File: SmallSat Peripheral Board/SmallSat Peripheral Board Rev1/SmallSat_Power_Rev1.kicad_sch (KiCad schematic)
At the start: 17 parts

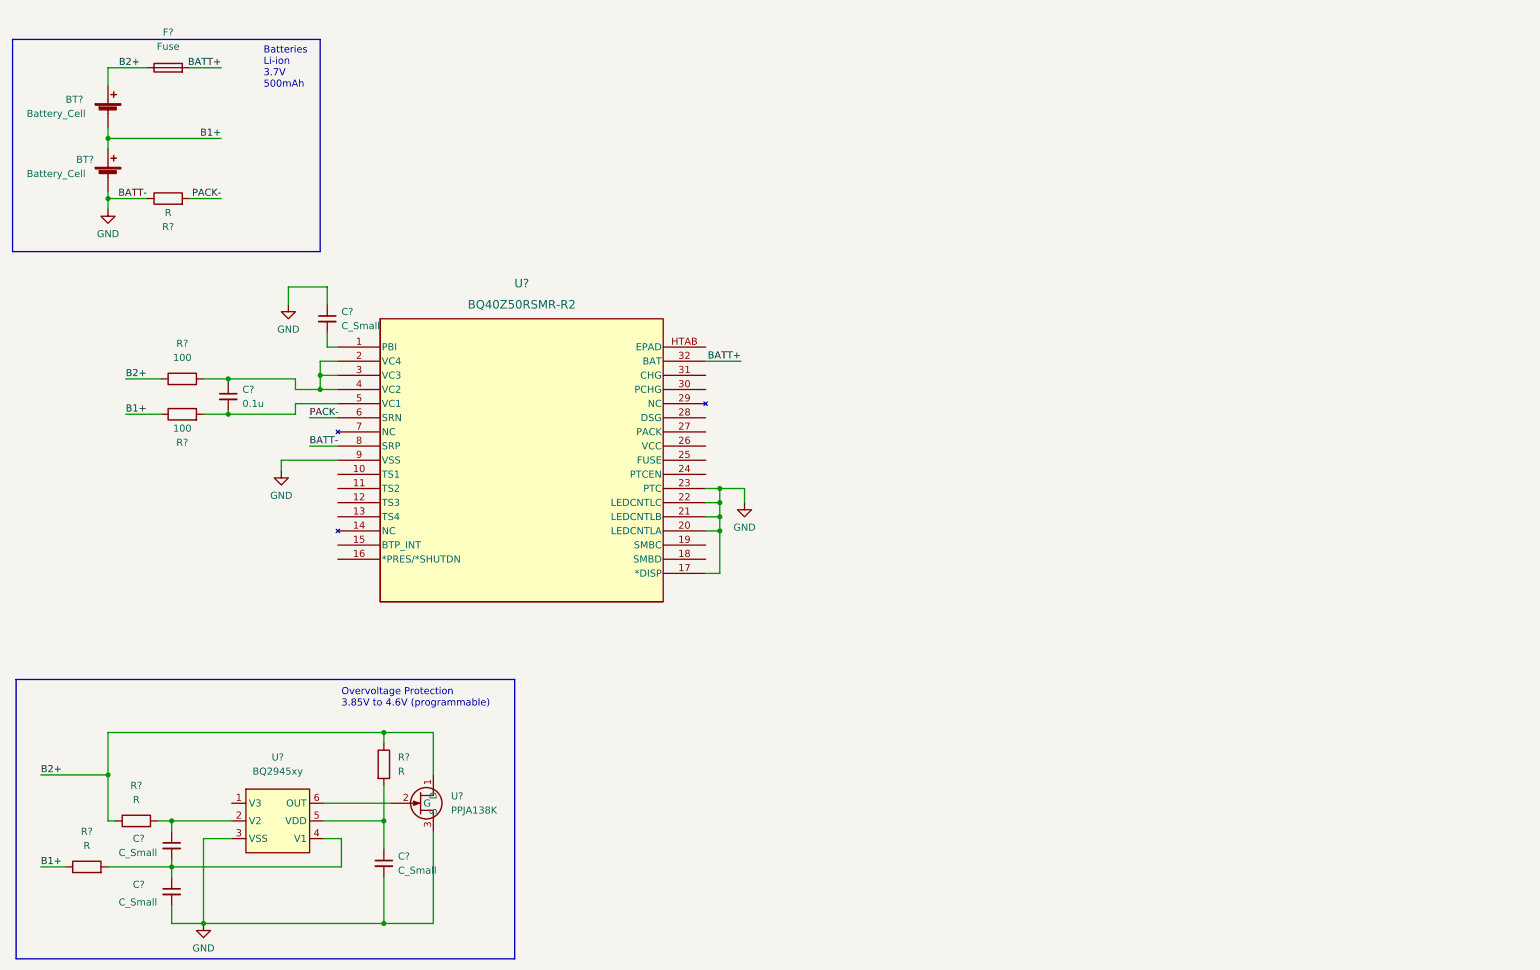
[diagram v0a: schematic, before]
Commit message: Updated Power Section
Now using BQ28Z620DRZR fuel gauge
Now using BQ296202DSGR protection
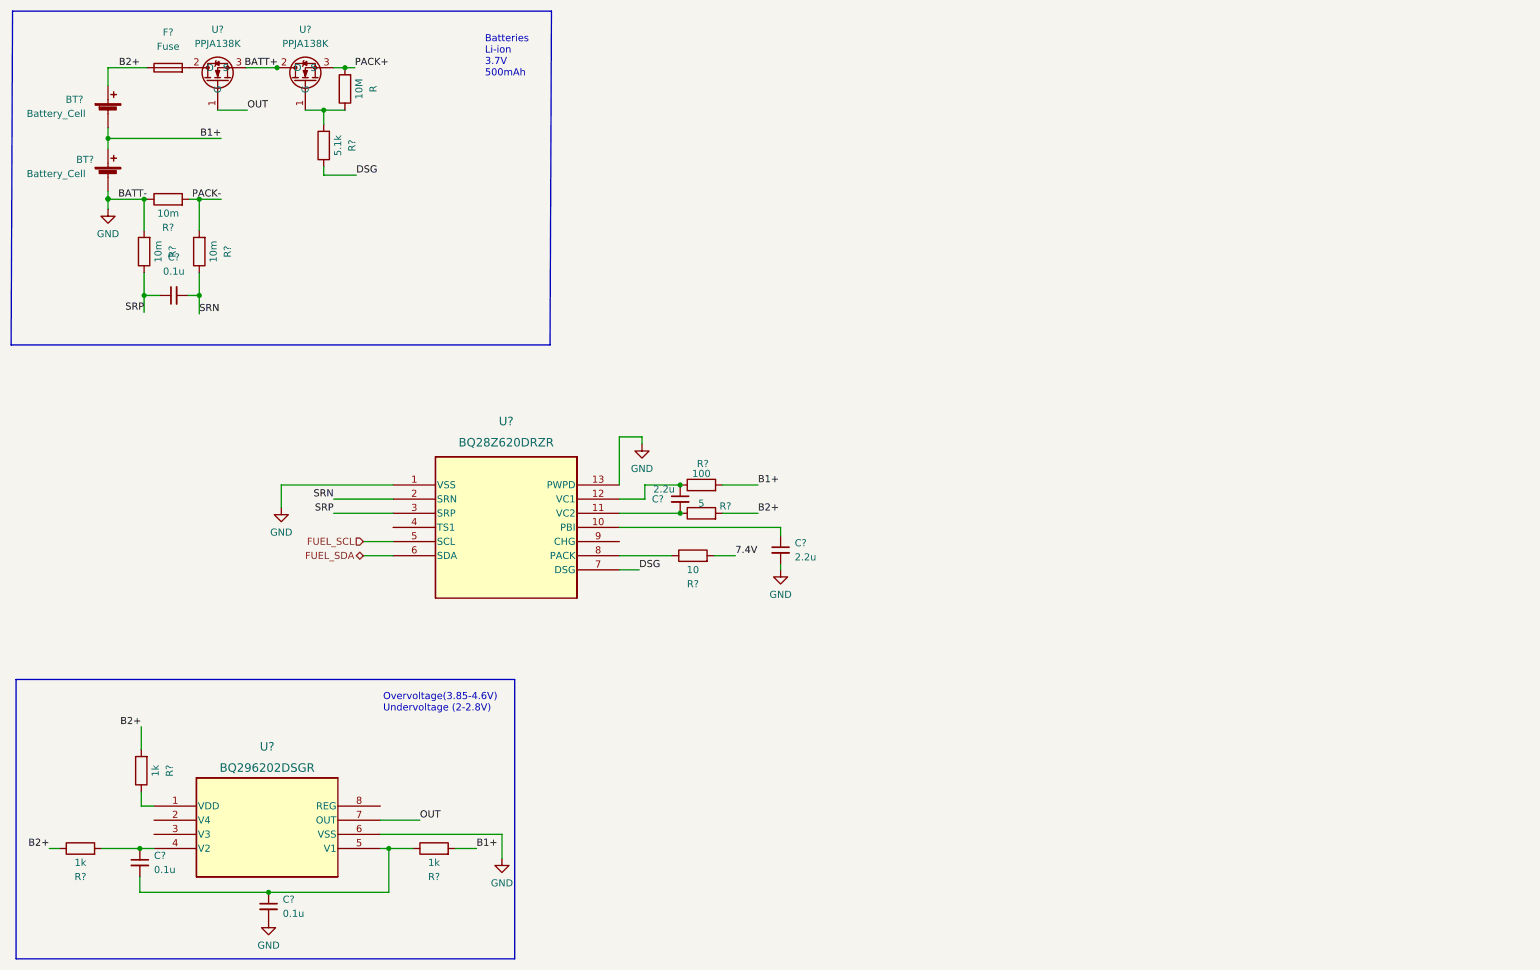
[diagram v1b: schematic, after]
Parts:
- removed C? (x4): C_Small, symbol Device:C_Small
- removed C?: 0.1u, symbol Device:C_Small
- removed R? (x2): 100, symbol Device:R
- removed R? (x3): R, symbol Device:R
- removed U?: BQ40Z50RSMR-R2, RSM32_1P5X1P5_TEX, symbol SmallSat-Peripherals-Board:BQ40Z50RSMR-R2
- removed U?: BQ2945xy, symbol SmallSat-Peripherals-Board:BQ2945xy
- removed U?: PPJA138K, symbol SmallSat-Peripherals-Board:PPJA138K
- added C? (x2): 2.2u, symbol Device:C_Small
- added C? (x3): 0.1u, symbol Device:C_Small
- added R: 10M, symbol Device:R
- added R? (x3): 1k, symbol Device:R
- added R?: 10, symbol Device:R
- added R? (x2): 10m, symbol Device:R
- added R?: 5, symbol Device:R
- added R?: 5.1k, symbol Device:R
- added R?: 100, symbol Device:R
- added U? (x2): PPJA138K, symbol SmallSat-Peripherals-Board:PPJA138K
- added U?: BQ296202DSGR, DSG8_TEX, symbol SmallSat-Peripherals-Board:BQ296202DSGR
- added U?: BQ28Z620DRZR, VSON12_DRZ_TEX, symbol SmallSat-Peripherals-Board:BQ28Z620DRZR
- R?: value R -> 10m
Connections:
- net B1+: now also R?.2, R?.2
- net B2+: now also R?.1, R?.2, R?.2
- net BATT+: now also U?.2 (D), U?.3 (S); no longer F?.2
- net GND: now also C?.2, C?.2, R?.2, U?.1 (VSS), U?.13 (PWPD), U?.6 (VSS)
- net PACK-: now also R?.2
- new net: C?.1, R?.2, U?.4 (V2)
- new net: R.1, R?.2, U?.1 (G)
- new net: R?.1, U?.1 (VDD)
- new net: C?.1, C?.2, R?.1, U?.5 (V1)
- new net: R?.1, U?.8 (PACK)
- new net: C?.1, R?.1, U?.12 (VC1)
- new net: C?.2, R?.1, U?.11 (VC2)
- new net: C?.1, U?.10 (PBI)
- new net: F?.2, U?.2 (D)
- new net 7.4V: R?.2
- new net DSG: R?.1, U?.7 (DSG)
- new net FUEL_SCL: U?.5 (SCL)
- new net FUEL_SDA: U?.6 (SDA)
- new net OUT: U?.1 (G), U?.7 (OUT)
- new net PACK+: R.2, U?.3 (S)
- new net SRN: C?.2, R?.1, U?.2 (SRN)
- new net SRP: C?.1, R?.1, U?.3 (SRP)
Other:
- note added: "Overvoltage(3.85-4.6V) Undervoltage (2-2.8V)"
- note removed: "Overvoltage Protection 3.85V to 4.6V (programmable)"

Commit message: Finished First Try for Power Board
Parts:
- added C? (x6): 22u, symbol Device:C
- added L? (x2): 2.2u, symbol Device:L
- added R, R?: 24.9k, symbol Device:R
- added R: 113k, symbol Device:R
- added R?: 182k, symbol Device:R
- added U? (x2): TPS62993QRYTRQ1, RYT0009A-MFG, symbol SmallSat-Peripherals-Board:TPS62993QRYTRQ1
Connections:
- net GND: now also C?.2, C?.2, C?.2, C?.2, C?.2, C?.2, R.2, R?.2, U?.4 (GND), U?.4 (GND), U?.7 (MODE_S-CONF), U?.7 (MODE_S-CONF)
- net PACK+: now also C?.1, C?.1, U?.5 (EN), U?.5 (EN), U?.6 (VIN), U?.6 (VIN)
- new net: C?.1, U?.8 (SS_TR) (x2)
- new net: L?.2, U?.2 (SW) (x2)
- new net: R.1, R?.2, U?.9 (FB_VSET)
- new net: R.2, R?.1, U?.9 (FB_VSET)
- new net 3.3V: C?.1, L?.1, R.1, U?.3 (VOS)
- new net 5V: C?.1, L?.1, R?.1, U?.3 (VOS)
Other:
- note added: "Leave empty pad to change out capacitors to determine good rise time"
- note added: "Section 9.2.2.2, p.24 for resistor divider values"
- note added: "Table 9-3 for LC output filter Combination and values"
